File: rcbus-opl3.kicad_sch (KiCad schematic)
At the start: 33 parts, among them CON1 3.5mm jack, P1 RC2014 BUS, U1 74HCT688, U2 YMF262, U3 YAC512, U4 TL074, Y1 14.3181MHz

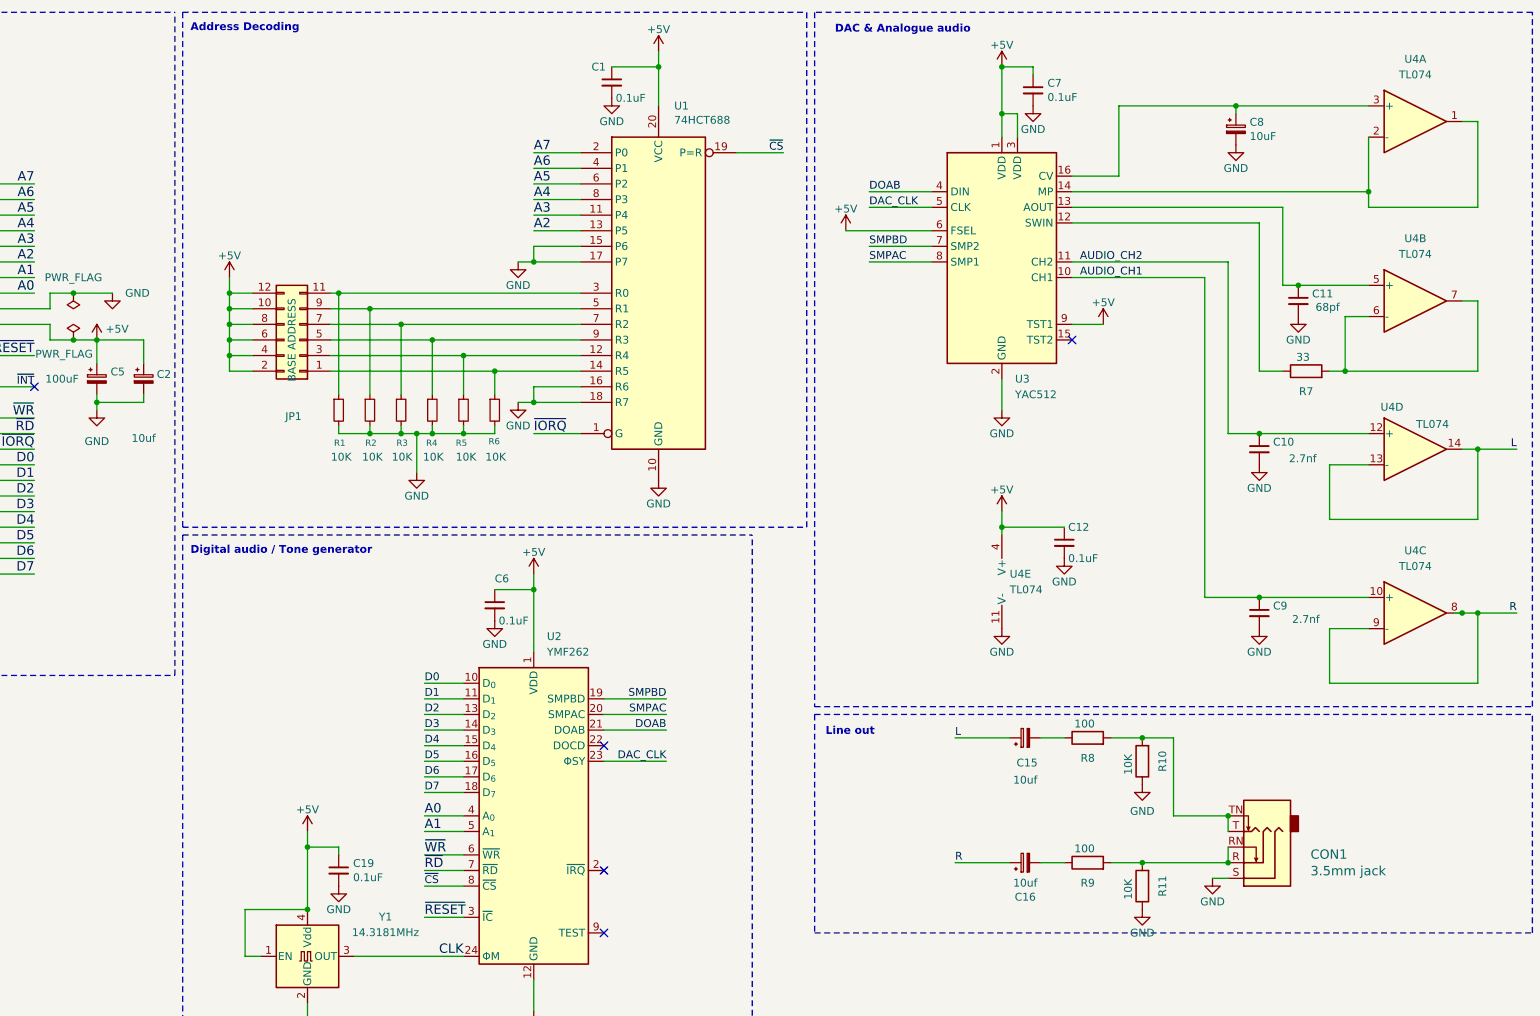
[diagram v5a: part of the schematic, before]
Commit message: add stitching vias
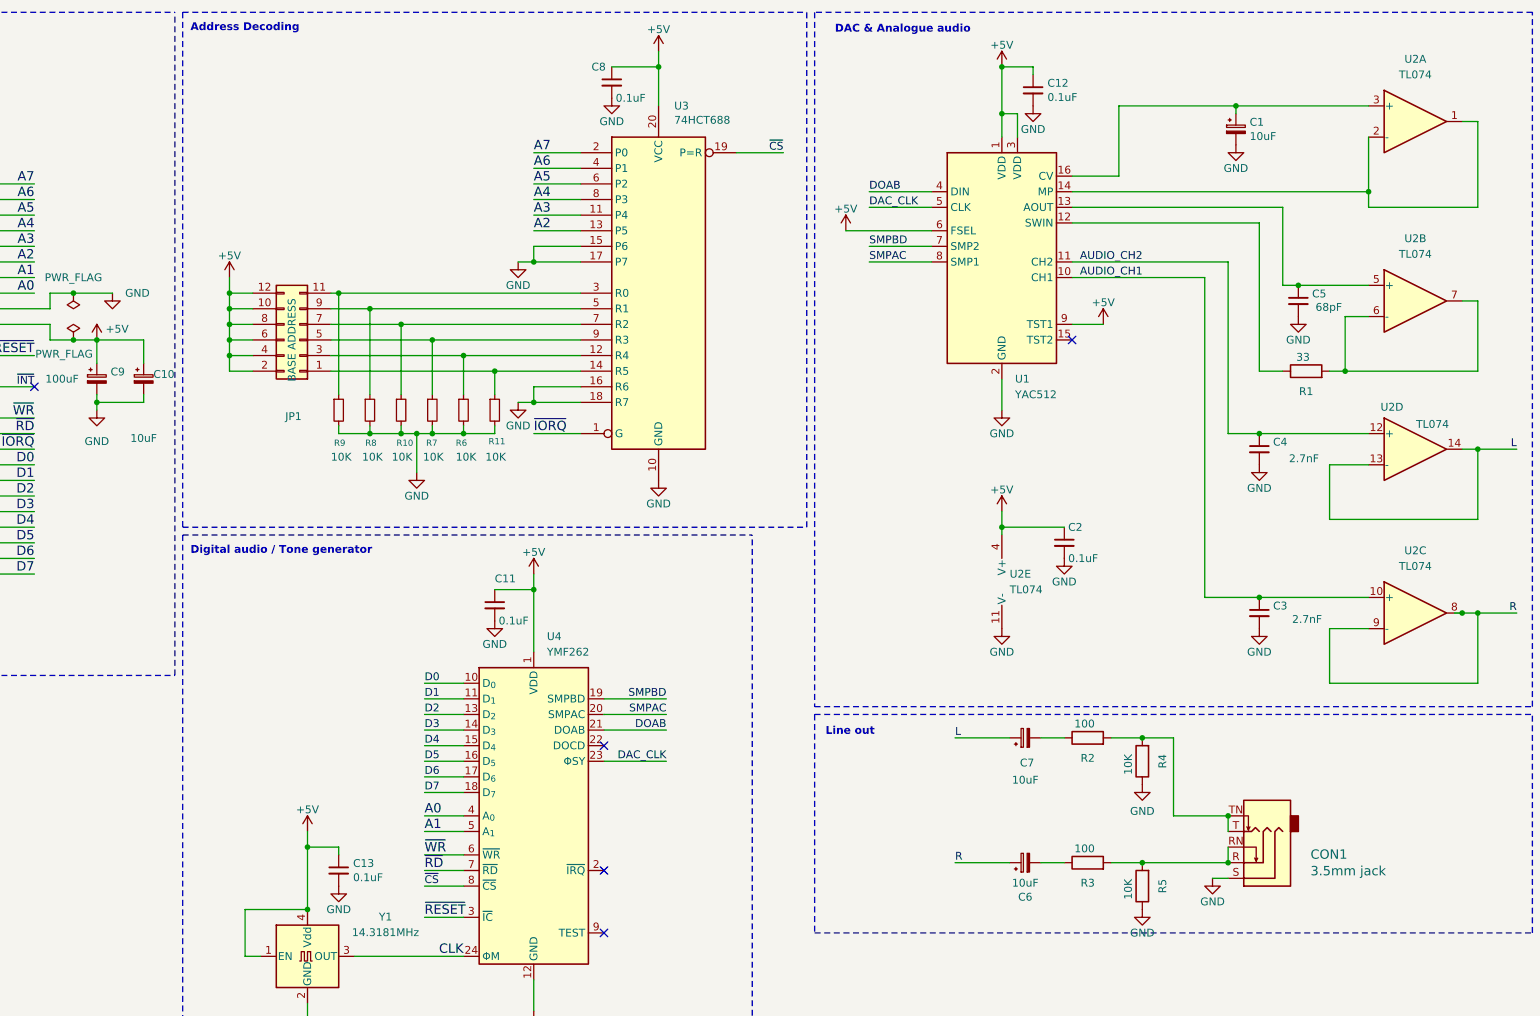
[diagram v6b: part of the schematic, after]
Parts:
- C10: renamed from C2; value 10uf -> 10uF
- C3: renamed from C9; value 2.7nf -> 2.7nF
- C4: renamed from C10; value 2.7nf -> 2.7nF
- C5: renamed from C11; value 68pf -> 68pF
- C6: renamed from C16; value 10uf -> 10uF
- C7: renamed from C15; value 10uf -> 10uF
- renumbered C8 to C1, C6 to C11, C7 to C12, C19 to C13, C12 to C2, C1 to C8, C5 to C9, R7 to R1, R3 to R10, R6 to R11, R8 to R2, R9 to R3, R10 to R4, R11 to R5, R5 to R6, R4 to R7, R2 to R8, R1 to R9, U3 to U1, U4 to U2, U1 to U3, U2 to U4

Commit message: more tidyup
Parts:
- renumbered C6 to C2, C4 to C3, C3 to C4, C2 to C5, C5 to C6, R4 to R2, R2 to R3, R3 to R4, R7 to R6, R6 to R7, U2 to U1, U1 to U2
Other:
- moved on the sheet: H1
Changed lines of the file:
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@@
 	(text "Non-functional components"
 		(exclude_from_sim no)
-		(at 256.54 262.89 0)
+		(at 17.78 130.81 0)
 		(effects
 			(font
@@
 	(polyline
 		(pts
-			(xy 288.29 279.4) (xy 288.29 256.54)
+			(xy 49.53 147.32) (xy 49.53 124.46)
 		)
 		(stroke
@@
 	(polyline
 		(pts
-			(xy 252.73 256.54) (xy 288.29 256.54)
+			(xy 13.97 124.46) (xy 49.53 124.46)
 		)
 		(stroke
@@
 	(polyline
 		(pts
-			(xy 252.73 279.4) (xy 288.29 279.4)
+			(xy 13.97 147.32) (xy 49.53 147.32)
 		)
 		(stroke
@@
 	(polyline
 		(pts
-			(xy 252.73 256.54) (xy 252.73 279.4)
+			(xy 13.97 124.46) (xy 13.97 147.32)
 		)
 		(stroke
@@
 		(on_board yes)
 		(dnp no)
-		(property "Reference" "C2"
+		(property "Reference" "C5"
 			(at 206.375 97.79 0)
 			(effects
@@
 			(project ""
 				(path "/9a2d648d-863a-4b7b-80f9-d537185c212b"
-					(reference "C2")
+					(reference "C5")
 					(unit 1)
 				)
@@
 	(symbol
 		(lib_id "Mechanical:MountingHole")
-		(at 259.08 273.05 0)
+		(at 20.32 140.97 0)
 		(unit 1)
 		(exclude_from_sim no)
@@
 		(dnp no)
 		(property "Reference" "H1"
-			(at 261.62 271.8816 0)
+			(at 22.86 139.8016 0)
 			(effects
 				(font
@@
 		)
 		(property "Value" "MountingHole"
-			(at 261.62 274.193 0)
+			(at 22.86 142.113 0)
 			(effects
 				(font
@@
 		)
 		(property "Footprint" "MountingHole:MountingHole_3.2mm_M3"
-			(at 259.08 273.05 0)
+			(at 20.32 140.97 0)
 			(effects
 				(font
@@
 		)
 		(property "Datasheet" "~"
-			(at 259.08 273.05 0)
+			(at 20.32 140.97 0)
 			(effects
 				(font
@@
 		)
 		(property "Description" "Mounting Hole without connection"
-			(at 259.08 273.05 0)
+			(at 20.32 140.97 0)
 			(effects
 				(font
@@
 		(on_board yes)
 		(dnp no)
-		(property "Reference" "R4"
+		(property "Reference" "R2"
 			(at 221.742 135.89 90)
 			(effects
@@
 			(project "rcbus-opl3"
 				(path "/9a2d648d-863a-4b7b-80f9-d537185c212b"
-					(reference "R4")
+					(reference "R2")
 					(unit 1)
 				)
@@
 		(on_board yes)
 		(dnp no)
-		(property "Reference" "C3"
+		(property "Reference" "C4"
 			(at 239.7252 110.5916 0)
 			(effects
@@
 			(project "rc2014-ymf262"
 				(path "/9a2d648d-863a-4b7b-80f9-d537185c212b"
-					(reference "C3")
+					(reference "C4")
 					(unit 1)
 				)
@@
 		(on_board yes)
 		(dnp no)
-		(property "Reference" "U2"
+		(property "Reference" "U1"
 			(at 259.08 78.232 0)
 			(effects
@@
 			(project ""
 				(path "/9a2d648d-863a-4b7b-80f9-d537185c212b"
-					(reference "U2")
+					(reference "U1")
 					(unit 4)
 				)
@@
 		(dnp no)
 		(fields_autoplaced yes)
-		(property "Reference" "U2"
+		(property "Reference" "U1"
 			(at 262.89 50.8 0)
 			(effects
@@
 			(project ""
 				(path "/9a2d648d-863a-4b7b-80f9-d537185c212b"
-					(reference "U2")
+					(reference "U1")
 					(unit 2)
 				)
@@
 		(on_board yes)
 		(dnp no)
-		(property "Reference" "R6"
+		(property "Reference" "R7"
 			(at 106.68 84.074 0)
 			(effects
@@
 			(project ""
 				(path "/9a2d648d-863a-4b7b-80f9-d537185c212b"
-					(reference "R6")
+					(reference "R7")
 					(unit 1)
 				)
@@
 		(dnp no)
 		(fields_autoplaced yes)
-		(property "Reference" "U1"
+		(property "Reference" "U2"
 			(at 197.7233 73.66 0)
 			(effects
@@
 			(project ""
 				(path "/9a2d648d-863a-4b7b-80f9-d537185c212b"
-					(reference "U1")
+					(reference "U2")
 					(unit 1)
 				)
@@
 		(on_board yes)
 		(dnp no)
-		(property "Reference" "R2"
+		(property "Reference" "R3"
 			(at 209.55 135.382 90)
 			(effects
@@
 			(project "rcbus-opl3"
 				(path "/9a2d648d-863a-4b7b-80f9-d537185c212b"
-					(reference "R2")
+					(reference "R3")
 					(unit 1)
 				)
@@
 		(on_board yes)
 		(dnp no)
-		(property "Reference" "R3"
+		(property "Reference" "R4"
 			(at 209.55 155.702 90)
 			(effects
@@
 			(project "rcbus-opl3"
 				(path "/9a2d648d-863a-4b7b-80f9-d537185c212b"
-					(reference "R3")
+					(reference "R4")
 					(unit 1)
 				)
@@
 		(on_board yes)
 		(dnp no)
-		(property "Reference" "C5"
+		(property "Reference" "C6"
 			(at 246.0752 59.7916 0)
 			(effects
@@
 			(project "rc2014-ymf262"
 				(path "/9a2d648d-863a-4b7b-80f9-d537185c212b"
-					(reference "C5")
+					(reference "C6")
 					(unit 1)
 				)
@@
 		(on_board yes)
 		(dnp no)
-		(property "Reference" "C4"
+		(property "Reference" "C3"
 			(at 239.7252 83.9216 0)
 			(effects
@@
 			(project "rc2014-ymf262"
 				(path "/9a2d648d-863a-4b7b-80f9-d537185c212b"
-					(reference "C4")
+					(reference "C3")
 					(unit 1)
 				)
@@
 		(dnp no)
 		(fields_autoplaced yes)
-		(property "Reference" "U2"
+		(property "Reference" "U1"
 			(at 262.89 101.6 0)
 			(effects
@@
 			(project ""
 				(path "/9a2d648d-863a-4b7b-80f9-d537185c212b"
-					(reference "U2")
+					(reference "U1")
 					(unit 3)
 				)
@@
 		(on_board yes)
 		(dnp no)
-		(property "Reference" "C6"
+		(property "Reference" "C2"
 			(at 199.39 157.988 90)
 			(effects
@@
 			(project "rc2014-ymf262"
 				(path "/9a2d648d-863a-4b7b-80f9-d537185c212b"
-					(reference "C6")
+					(reference "C2")
 					(unit 1)
 				)
@@
 		(dnp no)
 		(fields_autoplaced yes)
-		(property "Reference" "U2"
+		(property "Reference" "U1"
 			(at 262.89 21.59 0)
 			(effects
@@
 			(project ""
 				(path "/9a2d648d-863a-4b7b-80f9-d537185c212b"
-					(reference "U2")
+					(reference "U1")
 					(unit 1)
 				)
@@
 		(dnp no)
 		(fields_autoplaced yes)
-		(property "Reference" "U2"
+		(property "Reference" "U1"
 			(at 196.85 105.4099 0)
 			(effects
@@
 			(project ""
 				(path "/9a2d648d-863a-4b7b-80f9-d537185c212b"
-					(reference "U2")
+					(reference "U1")
 					(unit 5)
 				)
@@
 		(on_board yes)
 		(dnp no)
-		(property "Reference" "R7"
+		(property "Reference" "R6"
 			(at 101.854 84.074 0)
 			(effects
@@
 			(project ""
 				(path "/9a2d648d-863a-4b7b-80f9-d537185c212b"
-					(reference "R7")
+					(reference "R6")
 					(unit 1)
 				)

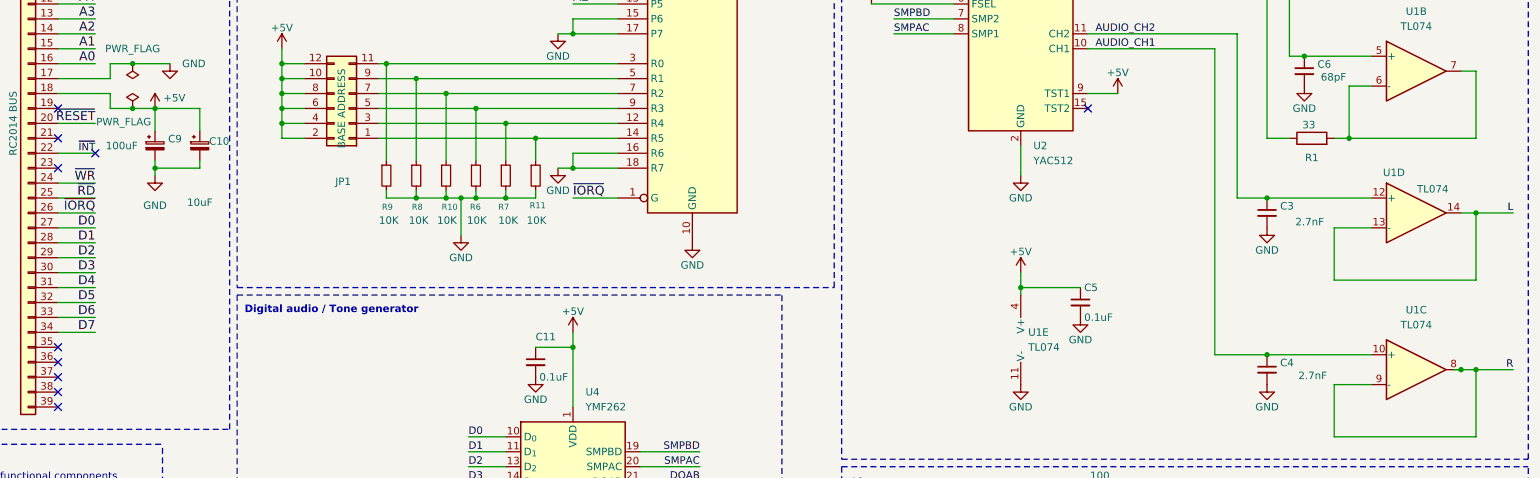
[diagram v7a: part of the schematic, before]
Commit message: sync up pcb and schematic, minor schematic tidyups
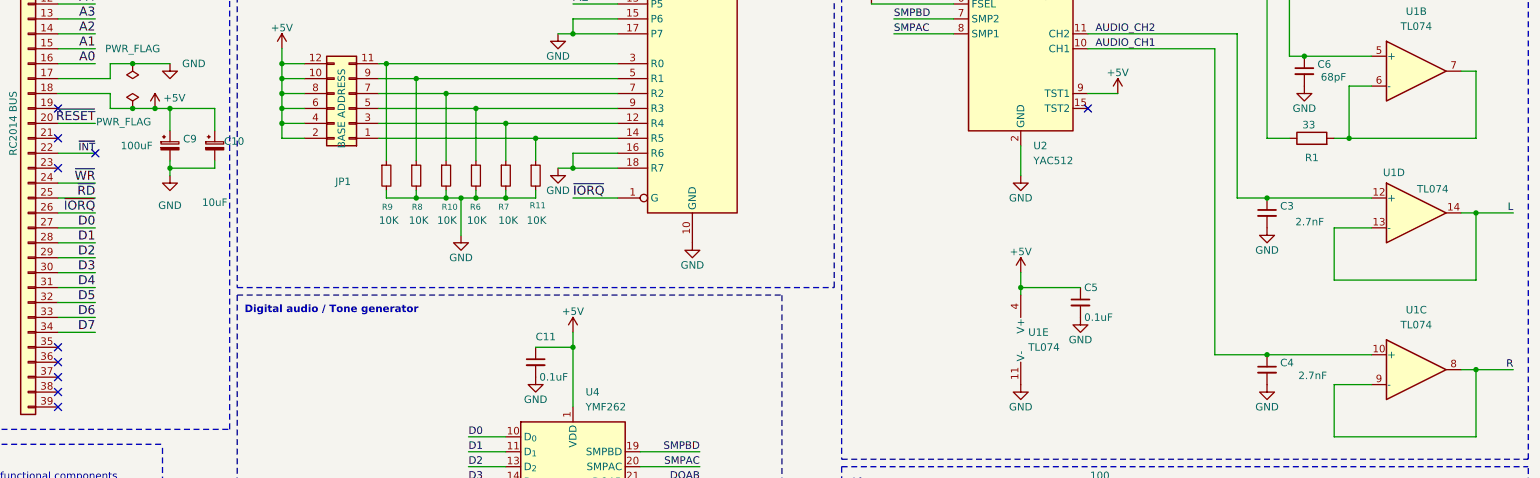
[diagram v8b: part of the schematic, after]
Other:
- moved on the sheet: C10, C9
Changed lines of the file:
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@@
 	)
 	(junction
-		(at 270.51 111.76)
-		(diameter 0)
-		(color 0 0 0 0)
-	)
-	(junction
-		(at 273.05 111.76)
-		(diameter 0)
-		(color 0 0 0 0)
-	)
-	(junction
 		(at 87.63 59.69)
 		(diameter 0)
@@
 	)
 	(junction
-		(at 48.26 67.31)
-		(diameter 0)
-		(color 0 0 0 0)
-	)
-	(junction
 		(at 69.85 69.85)
 		(diameter 0)
@@
 	)
 	(junction
+		(at 50.8 67.31)
+		(diameter 0)
+		(color 0 0 0 0)
+	)
+	(junction
 		(at 139.7 22.86)
 		(diameter 0)
@@
 	)
 	(junction
-		(at 48.26 77.47)
+		(at 50.8 77.47)
 		(diameter 0)
 		(color 0 0 0 0)
@@
 	)
 	(junction
+		(at 48.26 67.31)
+		(diameter 0)
+		(color 0 0 0 0)
+	)
+	(junction
 		(at 119.38 54.61)
 		(diameter 0)
@@
 	)
 	(junction
+		(at 273.05 111.76)
+		(diameter 0)
+		(color 0 0 0 0)
+	)
+	(junction
 		(at 92.71 62.23)
 		(diameter 0)
@@
 	(wire
 		(pts
-			(xy 48.26 71.12) (xy 48.26 67.31)
+			(xy 50.8 71.12) (xy 50.8 67.31)
 		)
 		(stroke
@@
 	(wire
 		(pts
+			(xy 270.51 111.76) (xy 273.05 111.76)
+		)
+		(stroke
+			(width 0)
+			(type default)
+		)
+	)
+	(wire
+		(pts
 			(xy 44.45 59.69) (xy 50.8 59.69)
 		)
@@
 	(wire
 		(pts
-			(xy 55.88 76.2) (xy 55.88 77.47)
+			(xy 58.42 76.2) (xy 58.42 77.47)
 		)
 		(stroke
@@
 	(wire
 		(pts
-			(xy 269.24 111.76) (xy 270.51 111.76)
-		)
-		(stroke
-			(width 0)
-			(type default)
-		)
-	)
-	(wire
-		(pts
 			(xy 87.63 82.55) (xy 92.71 82.55)
 		)
@@
 	(wire
 		(pts
-			(xy 48.26 77.47) (xy 55.88 77.47)
+			(xy 50.8 77.47) (xy 58.42 77.47)
 		)
 		(stroke
@@
 	(wire
 		(pts
-			(xy 48.26 76.2) (xy 48.26 77.47)
+			(xy 50.8 76.2) (xy 50.8 77.47)
 		)
 		(stroke
@@
 	(wire
 		(pts
+			(xy 48.26 67.31) (xy 50.8 67.31)
+		)
+		(stroke
+			(width 0)
+			(type default)
+		)
+	)
+	(wire
+		(pts
 			(xy 248.92 87.63) (xy 255.27 87.63)
 		)
@@
 	(wire
 		(pts
-			(xy 48.26 77.47) (xy 48.26 78.74)
+			(xy 50.8 77.47) (xy 50.8 78.74)
 		)
 		(stroke
@@
 	(wire
 		(pts
-			(xy 55.88 71.12) (xy 55.88 67.31)
+			(xy 58.42 71.12) (xy 58.42 67.31)
 		)
 		(stroke
@@
 	(wire
 		(pts
-			(xy 55.88 67.31) (xy 48.26 67.31)
+			(xy 58.42 67.31) (xy 50.8 67.31)
 		)
 		(stroke
@@
 	(wire
 		(pts
-			(xy 270.51 111.76) (xy 273.05 111.76)
-		)
-		(stroke
-			(width 0)
-			(type default)
-		)
-	)
-	(wire
-		(pts
 			(xy 273.05 72.39) (xy 273.05 60.96)
 		)
@@
 	(symbol
 		(lib_id "Device:C_Polarized_Small")
-		(at 48.26 73.66 0)
+		(at 50.8 73.66 0)
 		(unit 1)
 		(exclude_from_sim no)
@@
 		(dnp no)
 		(property "Reference" "C9"
-			(at 50.4952 72.4916 0)
+			(at 53.0352 72.4916 0)
 			(effects
 				(font
@@
 		)
 		(property "Value" "100uF"
-			(at 39.878 73.66 0)
+			(at 42.418 73.66 0)
 			(effects
 				(font
@@
 		)
 		(property "Footprint" "Capacitor_SMD:CP_Elec_6.3x7.7"
-			(at 48.26 73.66 0)
+			(at 50.8 73.66 0)
 			(effects
 				(font
@@
 		)
 		(property "Datasheet" "~"
-			(at 48.26 73.66 0)
+			(at 50.8 73.66 0)
 			(effects
 				(font
@@
 		)
 		(property "Description" "Polarized capacitor, small symbol"
-			(at 48.26 73.66 0)
+			(at 50.8 73.66 0)
 			(effects
 				(font
@@
 	(symbol
 		(lib_id "Device:C_Polarized_Small")
-		(at 55.88 73.66 0)
+		(at 58.42 73.66 0)
 		(unit 1)
 		(exclude_from_sim no)
@@
 		(dnp no)
 		(property "Reference" "C10"
-			(at 59.182 72.898 0)
+			(at 61.722 72.898 0)
 			(effects
 				(font
@@
 		)
 		(property "Value" "10uF"
-			(at 55.88 83.312 0)
+			(at 58.42 83.312 0)
 			(effects
 				(font
@@
 		)
 		(property "Footprint" "Capacitor_SMD:CP_Elec_6.3x5.8"
-			(at 55.88 73.66 0)
+			(at 58.42 73.66 0)
 			(effects
 				(font
@@
 		)
 		(property "Datasheet" "~"
-			(at 55.88 73.66 0)
+			(at 58.42 73.66 0)
 			(effects
 				(font
@@
 		)
 		(property "Description" "Polarized capacitor, small symbol"
-			(at 55.88 73.66 0)
+			(at 58.42 73.66 0)
 			(effects
 				(font
@@
 	(symbol
 		(lib_id "power:GND")
-		(at 48.26 78.74 0)
+		(at 50.8 78.74 0)
 		(unit 1)
 		(exclude_from_sim no)
@@
 		(fields_autoplaced yes)
 		(property "Reference" "#PWR017"
-			(at 48.26 85.09 0)
+			(at 50.8 85.09 0)
 			(effects
 				(font
@@
 		)
 		(property "Value" "GND"
-			(at 48.26 83.82 0)
+			(at 50.8 83.82 0)
 			(effects
 				(font
@@
 		)
 		(property "Footprint" ""
-			(at 48.26 78.74 0)
+			(at 50.8 78.74 0)
 			(effects
 				(font
@@
 		)
 		(property "Datasheet" ""
-			(at 48.26 78.74 0)
+			(at 50.8 78.74 0)
 			(effects
 				(font
@@
 		)
 		(property "Description" "Power symbol creates a global label with name \"GND\" , ground"
-			(at 48.26 78.74 0)
+			(at 50.8 78.74 0)
 			(effects
 				(font
